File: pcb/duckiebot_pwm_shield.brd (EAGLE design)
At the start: 66 x 56.2 mm, 10 parts, among them J1 RASPBERRYPI-40-PIN-GPIO

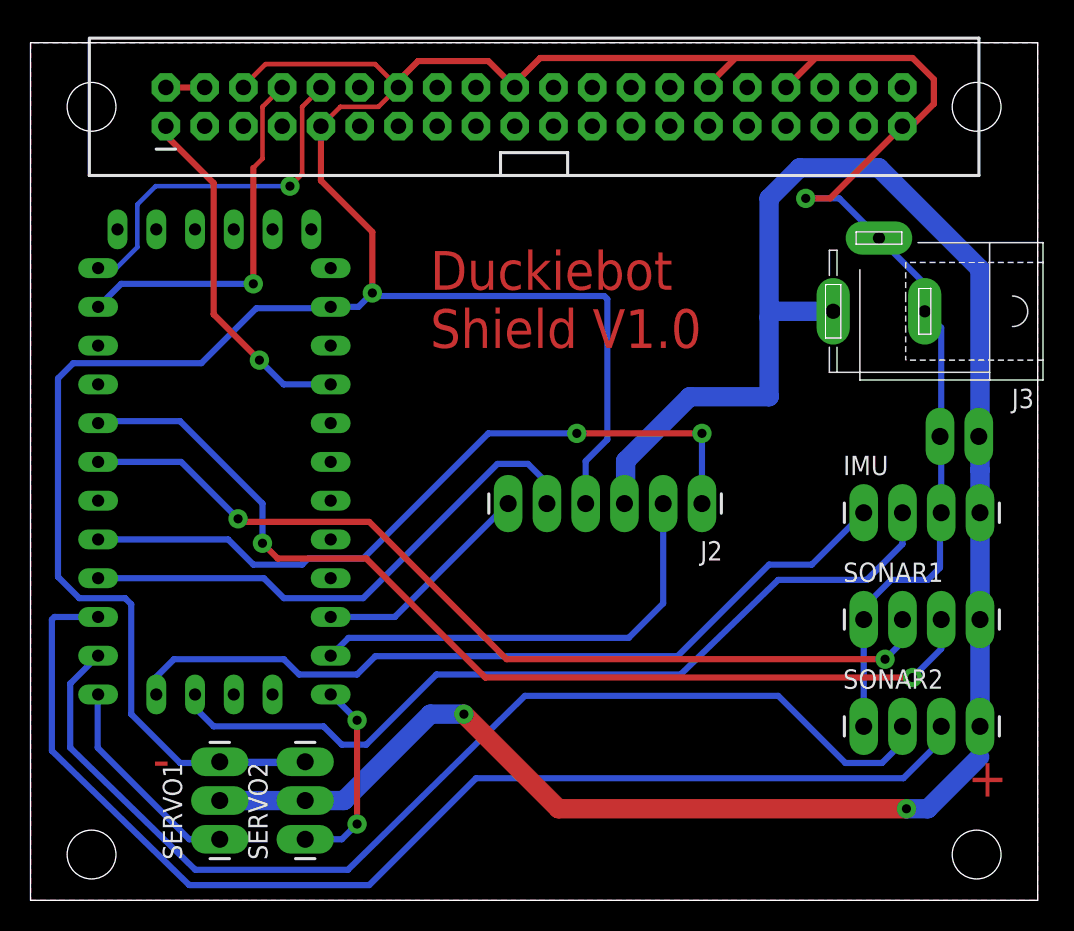
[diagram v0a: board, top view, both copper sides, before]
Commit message: duckiebot shield updated v1.1
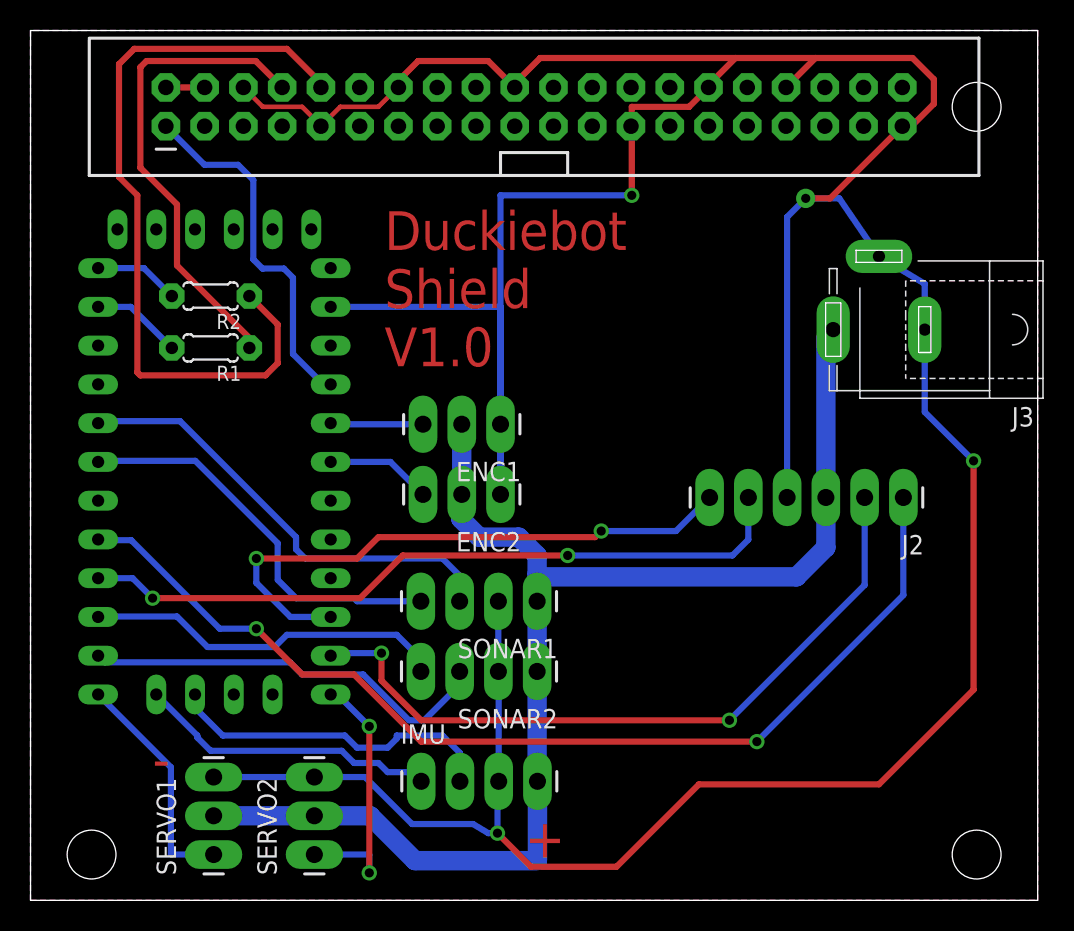
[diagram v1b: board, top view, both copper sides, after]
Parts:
- removed J5: (no value), SparkFun-Connectors:1X02_LONGPADS
- added ENC1, ENC2: (no value), SparkFun-Connectors:1X03_LONGPADS
- added R1, R2: 1k, adafruit:0204/5
- moved IMU 33.9 mm to (25.6, 7.80)
- moved SONAR2 21.7 mm to (33.2, 15.0), turned to 180 degrees
- moved SONAR1 21.4 mm to (33.2, 19.6), turned to 180 degrees
- moved J2 13.2 mm to (57.2, 26.4)
- moved J3 1.20 mm to (55.6, 37.4)
- moved SERVO2 1.17 mm to (18.6, 3.00)
- moved SERVO1 1.08 mm to (12.0, 3.00)
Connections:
- new net A2: ENC2.3, U$2.A2
- new net A3: ENC1.3, U$2.A3
- new net N$3: J1.10, R2.1
- new net N$4: J1.8, R1.1
- net D3: now also SONAR1.4; no longer SONAR1.2
- net D7: now also SONAR2.4; no longer SONAR2.3
- net D8: now also SONAR2.3; no longer SONAR2.2
- net GND: now also ENC1.1, ENC2.1, SONAR1.2, SONAR2.2; no longer J5.1, SONAR1.1, SONAR2.1
- net N$1: now also R1.2; no longer J1.8
- net N$2: now also R2.2; no longer J1.10
- net VCC: now also ENC1.2, ENC2.2, SONAR1.1, SONAR2.1; no longer J5.2, SONAR1.4, SONAR2.4
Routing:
- net D7: track 78.4 -> 23.8 mm
- net N$3: track 0.00 -> 50.3 mm
- net VCC: track 139.1 -> 90.1 mm, vias 2 -> 0
- net D8: track 72.7 -> 27.3 mm
- net D2: track 66.5 -> 30.1 mm, vias 2 -> 0
- net GND: track 226.0 -> 262.1 mm, vias 2 -> 4
- net D3: track 60.0 -> 26.4 mm, vias 2 -> 0
- net SCL: track 55.7 -> 22.1 mm
- net SDA: track 52.8 -> 19.9 mm
- net N$4: track 0.00 -> 31.5 mm
- net B-1A: track 14.7 -> 38.8 mm, vias 0 -> 2
- net A-1B: track 48.4 -> 68.6 mm
- net N$1: track 24.5 -> 5.94 mm, vias 1 -> 0
- net N$2: track 23.8 -> 5.59 mm, vias 1 -> 0
- net A-1A: track 29.8 -> 47.4 mm, vias 0 -> 2
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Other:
- board size 66 x 56.2 mm -> 66 x 57 mm

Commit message: duckiebot shield v1.2, duck missing :(
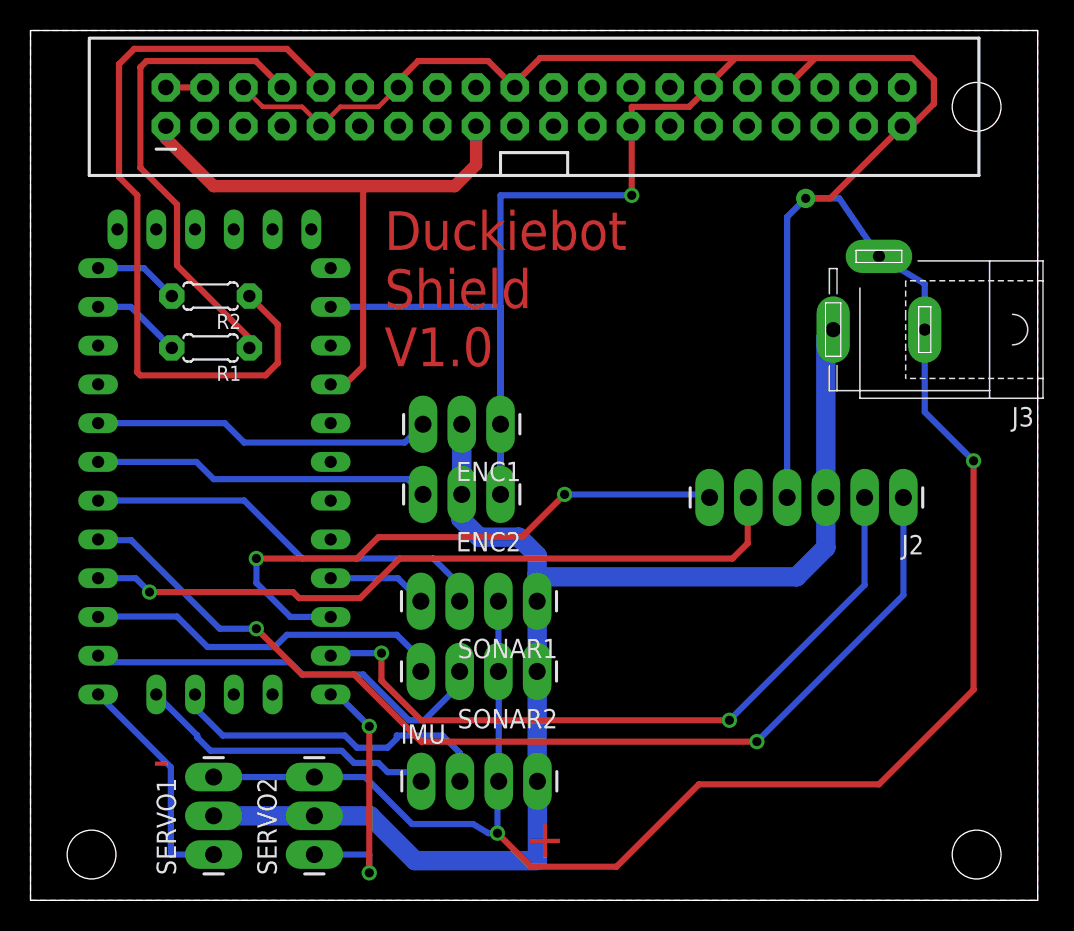
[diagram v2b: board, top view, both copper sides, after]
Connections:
- removed net A2: ENC2.3, U$2.A2
- removed net A3: ENC1.3, U$2.A3
- removed net N$5: J1.1, U$2.VCC
- new net D13: SONAR1.4, U$2.D13
- new net D4: SONAR1.3, U$2.D4
- net 3.3V: now also J1.1, U$2.VCC
- net D2: now also ENC1.3; no longer SONAR1.3
- net D3: now also ENC2.3; no longer SONAR1.4
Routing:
- net 3.3V: track 0.00 -> 40.0 mm
- net D4: track 0.00 -> 27.1 mm
- net N$5: track 23.8 -> 0.00 mm
- net D2: track 30.1 -> 22.3 mm
- net A2: track 6.93 -> 0.00 mm
- net D13: track 0.00 -> 6.54 mm
- net A3: track 6.08 -> 0.00 mm
- net D3: track 26.4 -> 22.2 mm
- net B-1B: track 47.5 -> 47.6 mm, vias 2 -> 1
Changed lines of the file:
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@@
 <signal name="3.3V">
 <contactref element="J1" pad="17"/>
+<contactref element="J1" pad="1"/>
+<contactref element="U$2" pad="VCC"/>
+<wire x1="8.87" y1="50.73" x2="8.87" y2="49.93" width="0.8128" layer="1"/>
+<wire x1="8.87" y1="49.93" x2="12" y2="46.8" width="0.8128" layer="1"/>
+<wire x1="12" y1="46.8" x2="22" y2="46.8" width="0.8128" layer="1"/>
+<wire x1="22" y1="46.8" x2="27.8" y2="46.8" width="0.8128" layer="1"/>
+<wire x1="27.8" y1="46.8" x2="29.2" y2="48.2" width="0.8128" layer="1"/>
+<wire x1="29.2" y1="48.2" x2="29.2" y2="50.72" width="0.8128" layer="1"/>
+<wire x1="29.2" y1="50.72" x2="29.19" y2="50.73" width="0.8128" layer="1"/>
+<wire x1="22" y1="46.8" x2="21.8" y2="46.6" width="0.4064" layer="1" curve="90"/>
+<wire x1="21.8" y1="46.6" x2="21.8" y2="35" width="0.4064" layer="1"/>
+<wire x1="21.8" y1="35" x2="20.61" y2="33.81" width="0.4064" layer="1"/>
+<wire x1="20.61" y1="33.81" x2="19.67" y2="33.81" width="0.4064" layer="1"/>
 </signal>
 <signal name="5V">
@@
 <signal name="RAW">
 <contactref element="U$2" pad="RAW"/>
-</signal>
-<signal name="N$5">
-<contactref element="J1" pad="1"/>
-<contactref element="U$2" pad="VCC"/>
-<wire x1="19.67" y1="33.81" x2="19.19" y2="33.81" width="0.4064" layer="16"/>
-<wire x1="19.19" y1="33.81" x2="17.2" y2="35.8" width="0.4064" layer="16"/>
-<wire x1="17.2" y1="35.8" x2="17.2" y2="40.8" width="0.4064" layer="16"/>
-<wire x1="17.2" y1="40.8" x2="16.6" y2="41.4" width="0.4064" layer="16"/>
-<wire x1="16.6" y1="41.4" x2="15.2" y2="41.4" width="0.4064" layer="16"/>
-<wire x1="15.2" y1="41.4" x2="14.6" y2="42" width="0.4064" layer="16"/>
-<wire x1="14.6" y1="42" x2="14.6" y2="47.2" width="0.4064" layer="16"/>
-<wire x1="14.6" y1="47.2" x2="13.6" y2="48.2" width="0.4064" layer="16"/>
-<wire x1="13.6" y1="48.2" x2="11.4" y2="48.2" width="0.4064" layer="16"/>
-<wire x1="11.4" y1="48.2" x2="8.87" y2="50.73" width="0.4064" layer="16"/>
 </signal>
 <signal name="N$2">
@@
 <contactref element="U$2" pad="D12"/>
 <contactref element="J2" pad="6"/>
-<wire x1="44.5" y1="26.4" x2="42.3" y2="24.2" width="0.4064" layer="16"/>
-<wire x1="42.3" y1="24.2" x2="37.4" y2="24.2" width="0.4064" layer="16"/>
-<via x="37.4" y="24.2" extent="1-16" drill="0.6" shape="square"/>
-<wire x1="37.4" y1="24.2" x2="37" y2="23.8" width="0.4064" layer="1"/>
-<wire x1="37" y1="23.8" x2="22.8" y2="23.8" width="0.4064" layer="1"/>
 <wire x1="22.8" y1="23.8" x2="21.4" y2="22.4" width="0.4064" layer="1"/>
 <wire x1="21.4" y1="22.4" x2="14.8" y2="22.4" width="0.4064" layer="1"/>
@@
 <via x="14.8" y="22.4" extent="1-16" drill="0.6" shape="square"/>
 <wire x1="14.8" y1="22.4" x2="14.8" y2="20.8" width="0.4064" layer="16"/>
+<wire x1="22.8" y1="23.8" x2="32.2" y2="23.8" width="0.4064" layer="1"/>
+<wire x1="32.2" y1="23.8" x2="35" y2="26.6" width="0.4064" layer="1"/>
+<via x="35" y="26.6" extent="1-16" drill="0.6" shape="square"/>
+<wire x1="35" y1="26.6" x2="44.3" y2="26.6" width="0.4064" layer="16"/>
+<wire x1="44.3" y1="26.6" x2="44.5" y2="26.4" width="0.4064" layer="16"/>
 </signal>
 <signal name="B-1B">
 <contactref element="U$2" pad="D6"/>
 <contactref element="J2" pad="5"/>
-<wire x1="47.04" y1="26.4" x2="47.04" y2="23.64" width="0.4064" layer="16"/>
-<wire x1="47.04" y1="23.64" x2="46" y2="22.6" width="0.4064" layer="16"/>
-<wire x1="46" y1="22.6" x2="35.2" y2="22.6" width="0.4064" layer="16"/>
-<via x="35.2" y="22.6" extent="1-16" drill="0.6" shape="square"/>
-<wire x1="35.2" y1="22.6" x2="24.4" y2="22.6" width="0.4064" layer="1"/>
-<wire x1="24.4" y1="22.6" x2="21.6" y2="19.8" width="0.4064" layer="1"/>
-<wire x1="21.6" y1="19.8" x2="8" y2="19.8" width="0.4064" layer="1"/>
-<via x="8" y="19.8" extent="1-16" drill="0.6" shape="square"/>
-<wire x1="8" y1="19.8" x2="6.69" y2="21.11" width="0.4064" layer="16"/>
-<wire x1="6.69" y1="21.11" x2="4.43" y2="21.11" width="0.4064" layer="16"/>
+<wire x1="4.43" y1="21.11" x2="6.89" y2="21.11" width="0.4064" layer="16"/>
+<wire x1="6.89" y1="21.11" x2="7.8" y2="20.2" width="0.4064" layer="16"/>
+<via x="7.8" y="20.2" extent="1-16" drill="0.6" shape="square"/>
+<wire x1="7.8" y1="20.2" x2="17.2" y2="20.2" width="0.4064" layer="1"/>
+<wire x1="17.2" y1="20.2" x2="17.6" y2="19.8" width="0.4064" layer="1"/>
+<wire x1="17.6" y1="19.8" x2="21.6" y2="19.8" width="0.4064" layer="1"/>
+<wire x1="21.6" y1="19.8" x2="24.2" y2="22.4" width="0.4064" layer="1"/>
+<wire x1="24.2" y1="22.4" x2="46" y2="22.4" width="0.4064" layer="1"/>
+<wire x1="46" y1="22.4" x2="47" y2="23.4" width="0.4064" layer="1"/>
+<wire x1="47" y1="23.4" x2="47" y2="26.36" width="0.4064" layer="1"/>
+<wire x1="47" y1="26.36" x2="47.04" y2="26.4" width="0.4064" layer="1"/>
 </signal>
 <signal name="A-1B">
@@
 <signal name="D2">
 <contactref element="U$2" pad="D2"/>
-<contactref element="SONAR1" pad="3"/>
-<wire x1="28.12" y1="19.6" x2="28.12" y2="21.28" width="0.4064" layer="16"/>
-<wire x1="28.12" y1="21.28" x2="27" y2="22.4" width="0.4064" layer="16"/>
-<wire x1="27" y1="22.4" x2="18" y2="22.4" width="0.4064" layer="16"/>
-<wire x1="18" y1="22.4" x2="17.4" y2="23" width="0.4064" layer="16"/>
-<wire x1="17.4" y1="23" x2="17.4" y2="23.8" width="0.4064" layer="16"/>
-<wire x1="17.4" y1="23.8" x2="9.8" y2="31.4" width="0.4064" layer="16"/>
-<wire x1="9.8" y1="31.4" x2="4.56" y2="31.4" width="0.4064" layer="16"/>
-<wire x1="4.56" y1="31.4" x2="4.43" y2="31.27" width="0.4064" layer="16"/>
+<contactref element="ENC1" pad="3"/>
+<wire x1="25.72" y1="31.2" x2="24.52" y2="30" width="0.4064" layer="16"/>
+<wire x1="24.52" y1="30" x2="14" y2="30" width="0.4064" layer="16"/>
+<wire x1="14" y1="30" x2="12.73" y2="31.27" width="0.4064" layer="16"/>
+<wire x1="12.73" y1="31.27" x2="4.43" y2="31.27" width="0.4064" layer="16"/>
 </signal>
 <signal name="D3">
 <contactref element="U$2" pad="D3"/>
-<contactref element="SONAR1" pad="4"/>
-<wire x1="25.58" y1="19.6" x2="21.4" y2="19.6" width="0.4064" layer="16"/>
-<wire x1="21.4" y1="19.6" x2="21.2" y2="19.8" width="0.4064" layer="16"/>
-<wire x1="21.2" y1="19.8" x2="17.4" y2="19.8" width="0.4064" layer="16"/>
-<wire x1="17.4" y1="19.8" x2="16.2" y2="21" width="0.4064" layer="16"/>
-<wire x1="16.2" y1="21" x2="16.2" y2="23.4" width="0.4064" layer="16"/>
-<wire x1="16.2" y1="23.4" x2="10.8" y2="28.8" width="0.4064" layer="16"/>
-<wire x1="10.8" y1="28.8" x2="4.5" y2="28.8" width="0.4064" layer="16"/>
-<wire x1="4.5" y1="28.8" x2="4.43" y2="28.73" width="0.4064" layer="16"/>
+<contactref element="ENC2" pad="3"/>
+<wire x1="25.72" y1="26.6" x2="24.72" y2="27.6" width="0.4064" layer="16"/>
+<wire x1="24.72" y1="27.6" x2="12" y2="27.6" width="0.4064" layer="16"/>
+<wire x1="12" y1="27.6" x2="10.87" y2="28.73" width="0.4064" layer="16"/>
+<wire x1="10.87" y1="28.73" x2="4.43" y2="28.73" width="0.4064" layer="16"/>
 </signal>
 <signal name="D7">
@@
 <wire x1="22.2" y1="11.4" x2="20.11" y2="13.49" width="0.4064" layer="16"/>
 <wire x1="20.11" y1="13.49" x2="19.67" y2="13.49" width="0.4064" layer="16"/>
-</signal>
-<signal name="A3">
-<contactref element="U$2" pad="A3"/>
-<contactref element="ENC1" pad="3"/>
-<wire x1="19.67" y1="31.27" x2="19.74" y2="31.2" width="0.4064" layer="16"/>
-<wire x1="19.74" y1="31.2" x2="25.72" y2="31.2" width="0.4064" layer="16"/>
-</signal>
-<signal name="A2">
-<contactref element="U$2" pad="A2"/>
-<contactref element="ENC2" pad="3"/>
-<wire x1="19.67" y1="28.73" x2="23.59" y2="28.73" width="0.4064" layer="16"/>
-<wire x1="23.59" y1="28.73" x2="25.72" y2="26.6" width="0.4064" layer="16"/>
 </signal>
 <signal name="N$3">
@@
 <wire x1="14.34" y1="36.86" x2="14.34" y2="36.2" width="0.4064" layer="1"/>
 </signal>
+<signal name="D13">
+<contactref element="U$2" pad="D13"/>
+<contactref element="SONAR1" pad="4"/>
+<wire x1="25.58" y1="19.6" x2="24.07" y2="21.11" width="0.4064" layer="16"/>
+<wire x1="24.07" y1="21.11" x2="19.67" y2="21.11" width="0.4064" layer="16"/>
+</signal>
+<signal name="D4">
+<contactref element="U$2" pad="D4"/>
+<contactref element="SONAR1" pad="3"/>
+<wire x1="28.12" y1="19.6" x2="28.12" y2="20.68" width="0.4064" layer="16"/>
+<wire x1="28.12" y1="20.68" x2="26.4" y2="22.4" width="0.4064" layer="16"/>
+<wire x1="26.4" y1="22.4" x2="17.8" y2="22.4" width="0.4064" layer="16"/>
+<wire x1="17.8" y1="22.4" x2="14" y2="26.2" width="0.4064" layer="16"/>
+<wire x1="14" y1="26.2" x2="4.44" y2="26.2" width="0.4064" layer="16"/>
+<wire x1="4.44" y1="26.2" x2="4.43" y2="26.19" width="0.4064" layer="16"/>
+</signal>
 </signals>
